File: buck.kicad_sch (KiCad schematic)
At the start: 32 parts, among them J6 Conn_01x02_Socket, Q1 RS1G120MNTB, Q2 RS1G120MNTB, U6 BQ24640

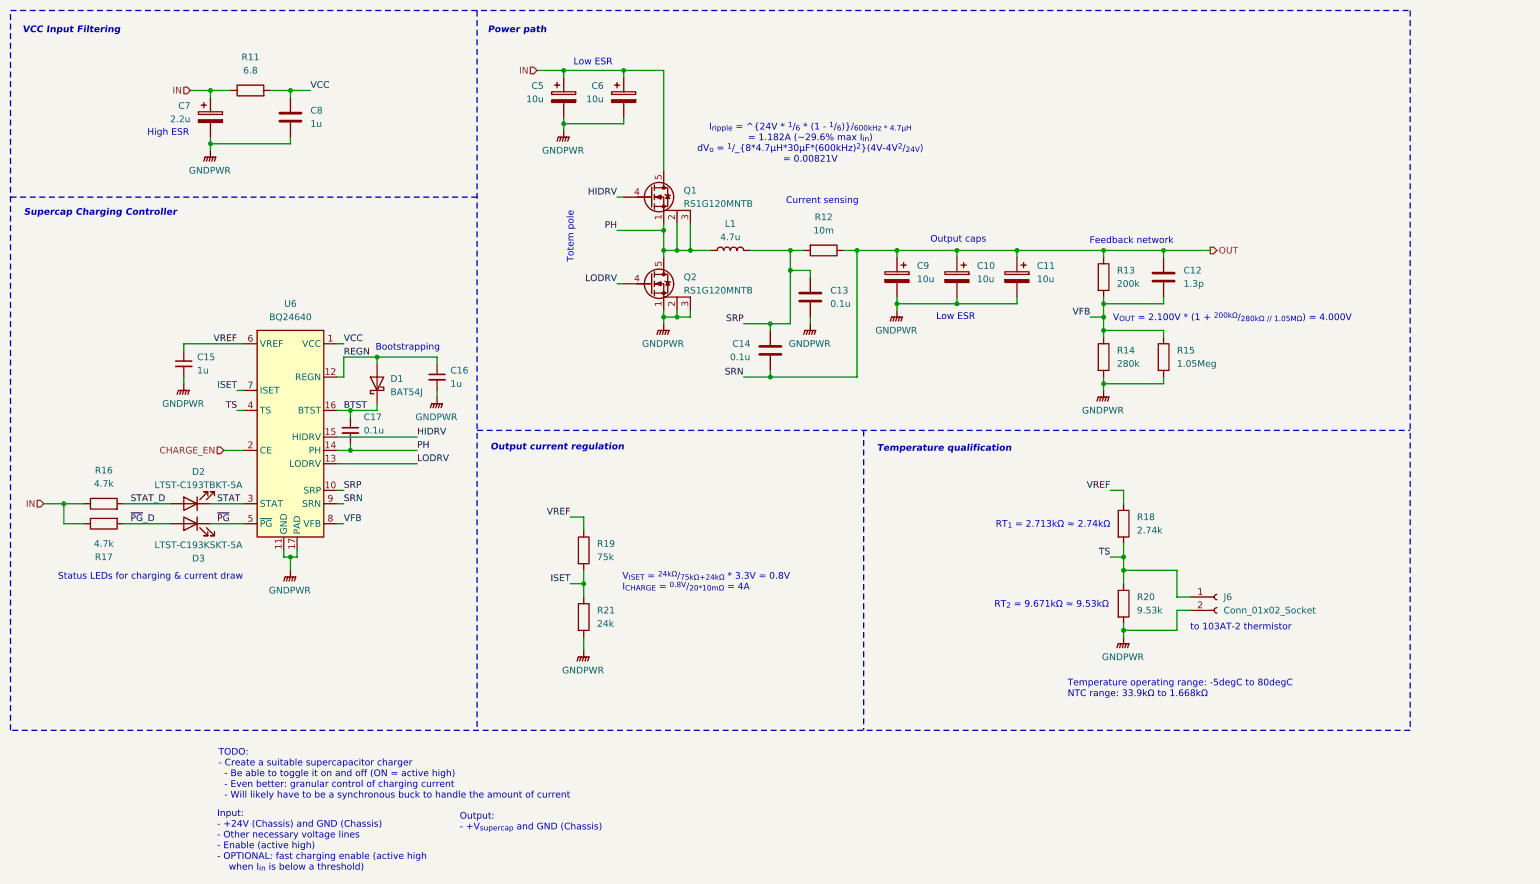
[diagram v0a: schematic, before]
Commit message: Tuned circuits & adjusted values
Changed footprints for some circuits to consolidate components
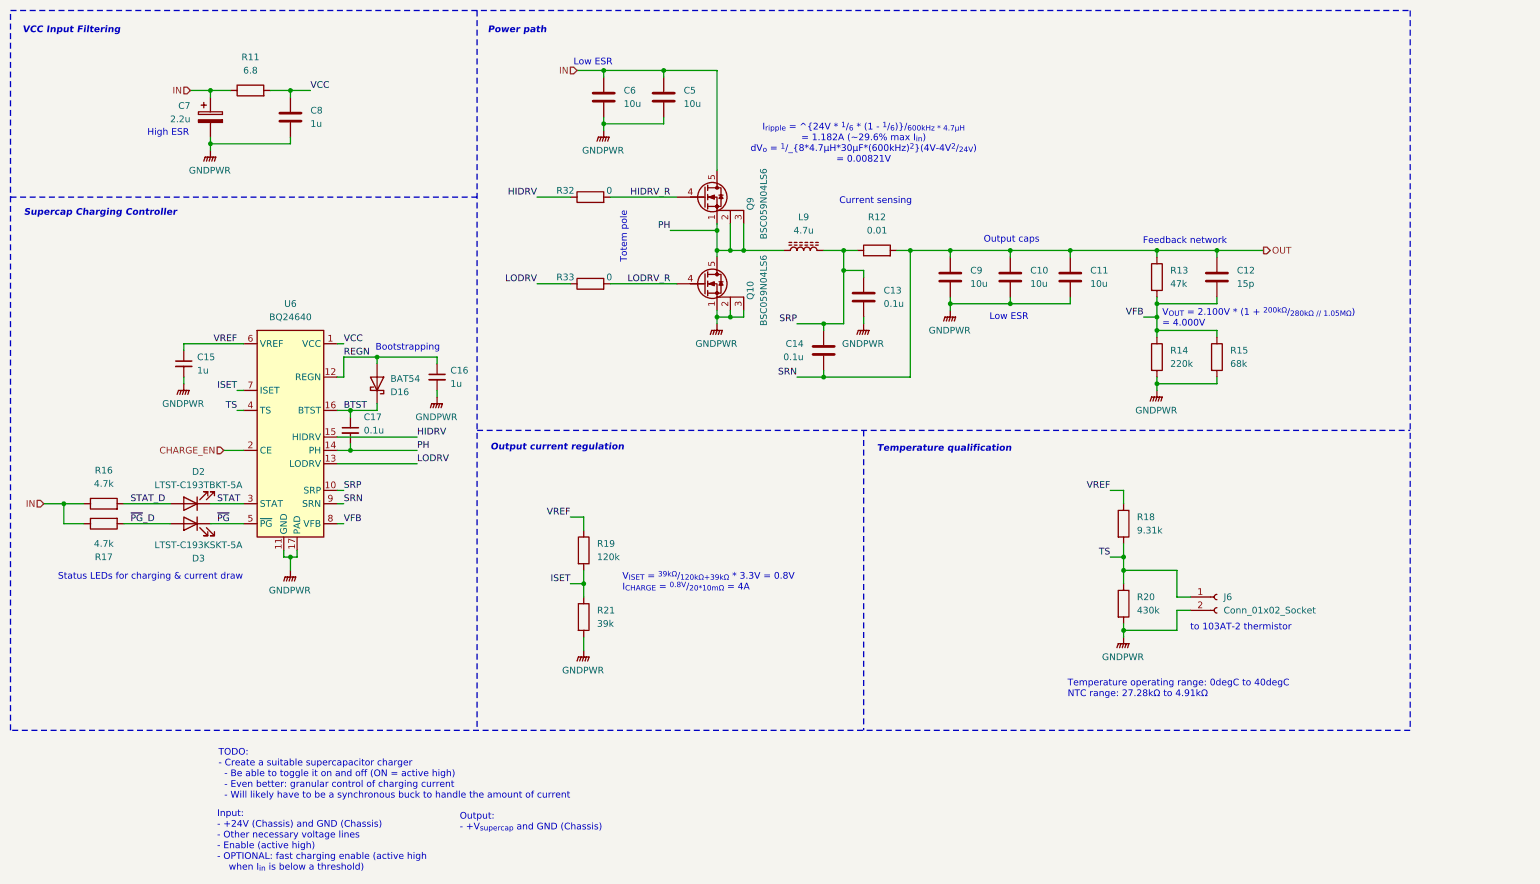
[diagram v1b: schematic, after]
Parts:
- removed C10, C11, C5, C6, C9: 10u, Capacitor_THT:CP_Radial_D5.0mm_P2.00mm, symbol Device:C_Polarized
- removed D1: BAT54J, Diode_SMD:D_SOD-323F, symbol Diode:BAT54J
- removed L1: 4.7u, Inductor_SMD:L_0603_1608Metric_Pad1.05x0.95mm_HandSolder, symbol Device:L
- removed Q1, Q2: RS1G120MNTB, Package_SO:PowerPAK_SO-8_Single, symbol Device:Q_NMOS_SGD
- added C10, C11, C5, C6, C9: 10u, Capacitor_SMD:C_0805_2012Metric_Pad1.18x1.45mm_HandSolder, symbol Device:C
- added D16: BAT54, Package_TO_SOT_SMD:SOT-23_Handsoldering, symbol Device:D_Schottky
- added L9: 4.7u, Inductor_SMD:L_Bourns_SRN8040TA, symbol Device:L_Ferrite
- added Q10, Q9: BSC059N04LS6, Package_SON:Infineon_PG-TDSON-8_6.15x5.15mm, symbol Transistor_FET:Q_NMOS_SGD
- added R32, R33: 0, Resistor_SMD:R_0603_1608Metric_Pad0.98x0.95mm_HandSolder, symbol Device:R
- C12: value 1.3p -> 15p
- C7: footprint Capacitor_SMD:C_0603_1608Metric_Pad1.08x0.95mm_HandSolder -> Capacitor_THT:C_Radial_D5.0mm_H11.0mm_P2.00mm; Mouser Part Number (none) -> 710-860010672006
- R12: value 10m -> 0.01; footprint Resistor_SMD:R_0603_1608Metric_Pad0.98x0.95mm_HandSolder -> Resistor_SMD:R_0612_1632Metric_Pad1.18x3.40mm_HandSolder; Mouser Part Number (none) -> 652-CFG0612FXR010ELF
- R13: value 200k -> 47k
- R14: value 280k -> 220k
- R15: value 1.05Meg -> 68k
- R18: value 2.74k -> 9.31k
- R19: value 75k -> 120k
- R20: value 9.53k -> 430k
- R21: value 24k -> 39k
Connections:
- net BTST: now also D16.3 (K)
- net GNDPWR: now also C10.2, C11.2, C5.2, C6.2, C9.2, Q10.1 (S), Q10.2 (S), Q10.3 (S)
- net HIDRV: now also R32.1
- net IN: now also C5.1, C6.1, Q9.5 (D)
- net LODRV: now also R33.1
- net OUT: now also R12.2, C10.1, C11.1, C9.1; no longer R12.1
- net PH: now also L9.1, Q10.5 (D), Q9.1 (S), Q9.2 (S), Q9.3 (S)
- net REGN: now also D16.1 (A)
- net SRP: now also R12.1, L9.2; no longer R12.2
- new net HIDRV_R: Q9.4 (G), R32.2
- new net LODRV_R: Q10.4 (G), R33.2
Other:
- note added: "Temperature operating range: 0degC to 40degC NTC range: 27.28kΩ to 4.91kΩ"
- note added: "V_{ISET} = ^{39kΩ}/_{120kΩ+39kΩ} * 3.3V = 0.8V I_{CHARGE} = ^{0.8V}/_{20*10mΩ} = 4A"
- note removed: "RT_{1} = 2.713kΩ ≈ 2.74kΩ"
- note removed: "RT_{2} = 9.671kΩ ≈ 9.53kΩ"
- note removed: "Temperature operating range: -5degC to 80degC NTC range: 33.9kΩ to 1.668kΩ"
- note removed: "V_{ISET} = ^{24kΩ}/_{75kΩ+24kΩ} * 3.3V = 0.8V I_{CHARGE} = ^{0.8V}/_{20*10mΩ} = 4A"
- moved on the sheet: C12, C13, C14, R13, R14, R15

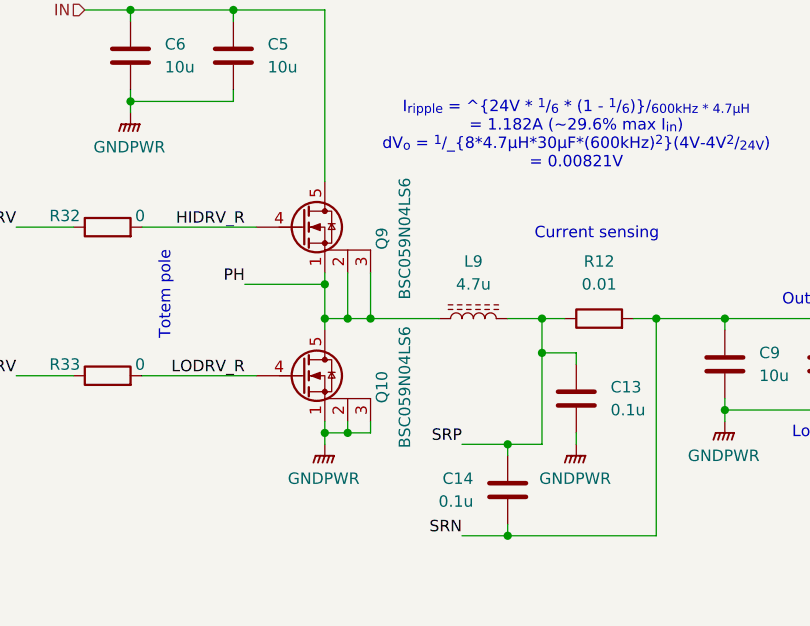
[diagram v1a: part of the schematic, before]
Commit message: Redesigning output boosts to be more efficient albeit with less current capacity
idk what I changed with the schematics lol
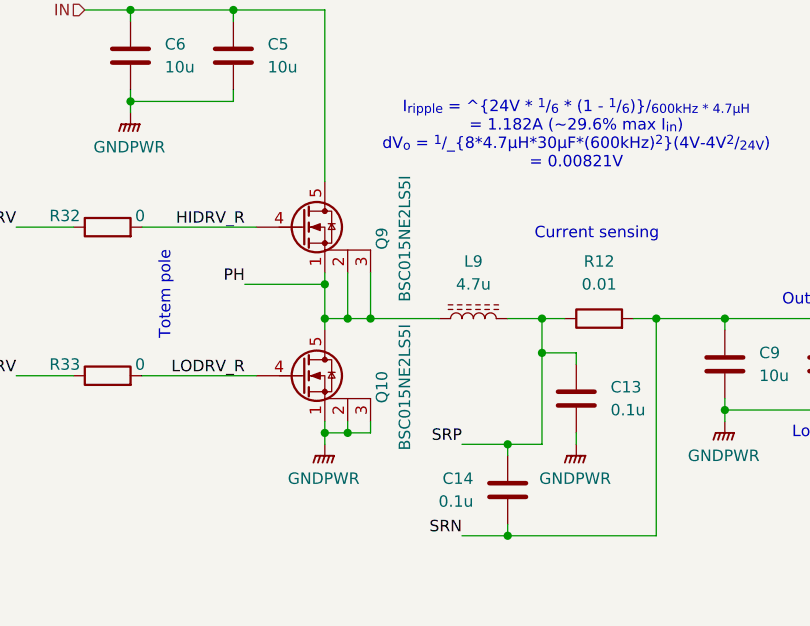
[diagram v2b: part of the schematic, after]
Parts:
- Q10, Q9: value BSC059N04LS6 -> BSC015NE2LS5I; Mouser Part Number 726-BSC059N04LS6ATMA -> 726-BSC015NE2LS5IATM
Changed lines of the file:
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@@
 			)
 		)
-		(property "Value" "BSC059N04LS6"
+		(property "Value" "BSC015NE2LS5I"
 			(at 157.48 60.96 90)
 			(effects
@@
 			)
 		)
-		(property "Datasheet" "https://www.mouser.com/datasheet/2/196/Infineon_BSC059N04LS6_DataSheet_v02_01_EN-3360636.pdf"
+		(property "Datasheet" "https://www.mouser.com/datasheet/2/196/Infineon_BSC015NE2LS5I_DataSheet_v02_01_EN-3360635.pdf"
 			(at 146.05 59.69 0)
 			(effects
@@
 			)
 		)
-		(property "Mouser Part Number" "726-BSC059N04LS6ATMA"
+		(property "Mouser Part Number" "726-BSC015NE2LS5IATM"
 			(at 146.05 59.69 0)
 			(effects
@@
 			)
 		)
-		(property "Value" "BSC059N04LS6"
+		(property "Value" "BSC015NE2LS5I"
 			(at 157.48 77.47 90)
 			(effects
@@
 			)
 		)
-		(property "Datasheet" "https://www.mouser.com/datasheet/2/196/Infineon_BSC059N04LS6_DataSheet_v02_01_EN-3360636.pdf"
+		(property "Datasheet" "https://www.mouser.com/datasheet/2/196/Infineon_BSC015NE2LS5I_DataSheet_v02_01_EN-3360635.pdf"
 			(at 146.05 76.2 0)
 			(effects
@@
 			)
 		)
-		(property "Mouser Part Number" "726-BSC059N04LS6ATMA"
+		(property "Mouser Part Number" "726-BSC015NE2LS5IATM"
 			(at 146.05 76.2 0)
 			(effects

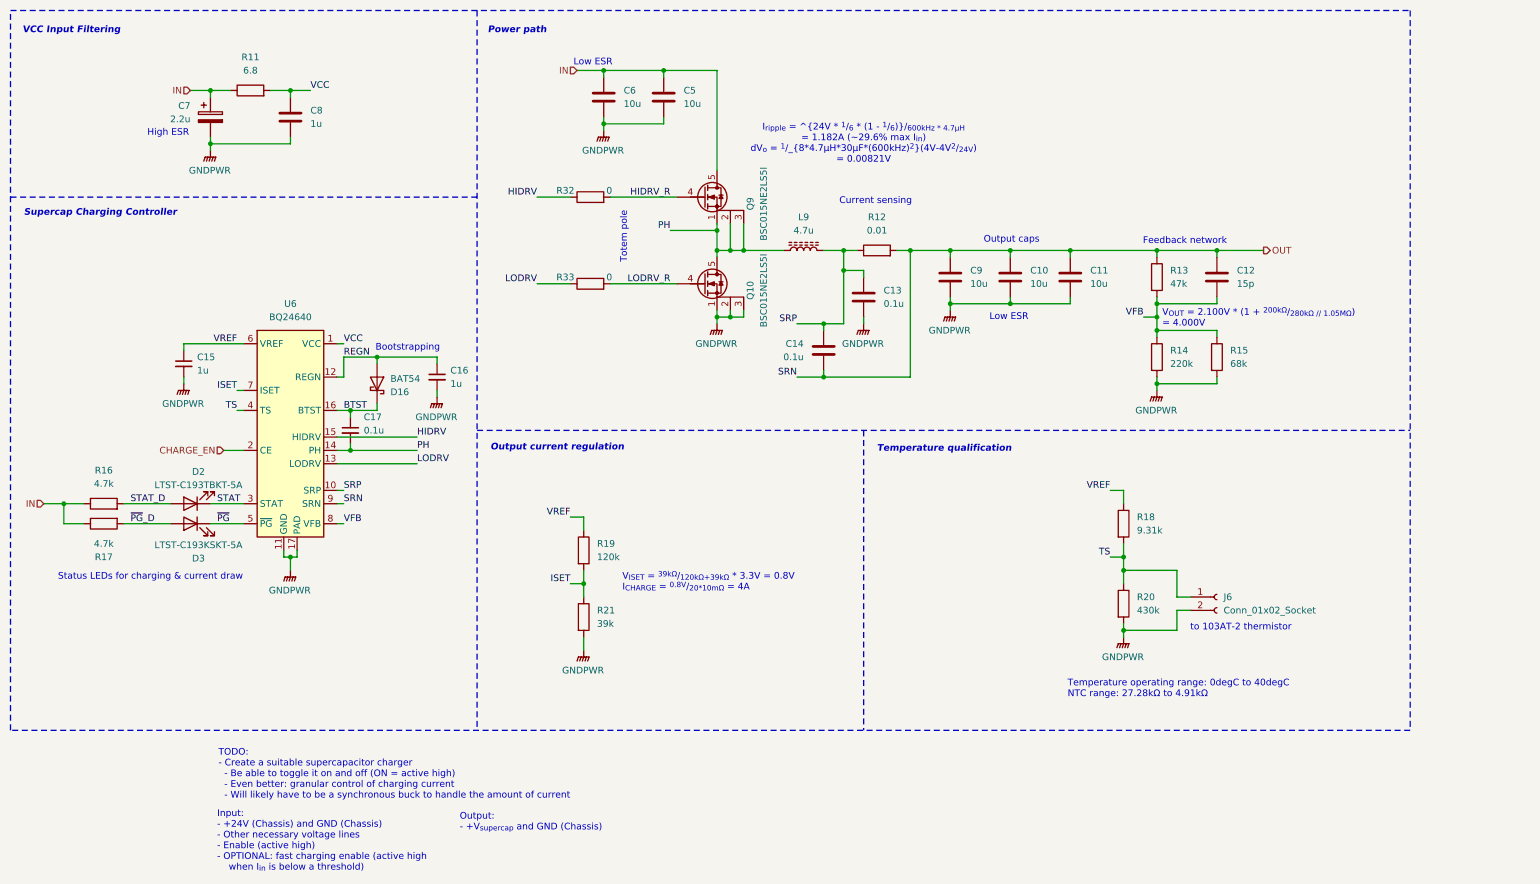
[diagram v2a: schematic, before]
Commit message: Up charging current to 6A
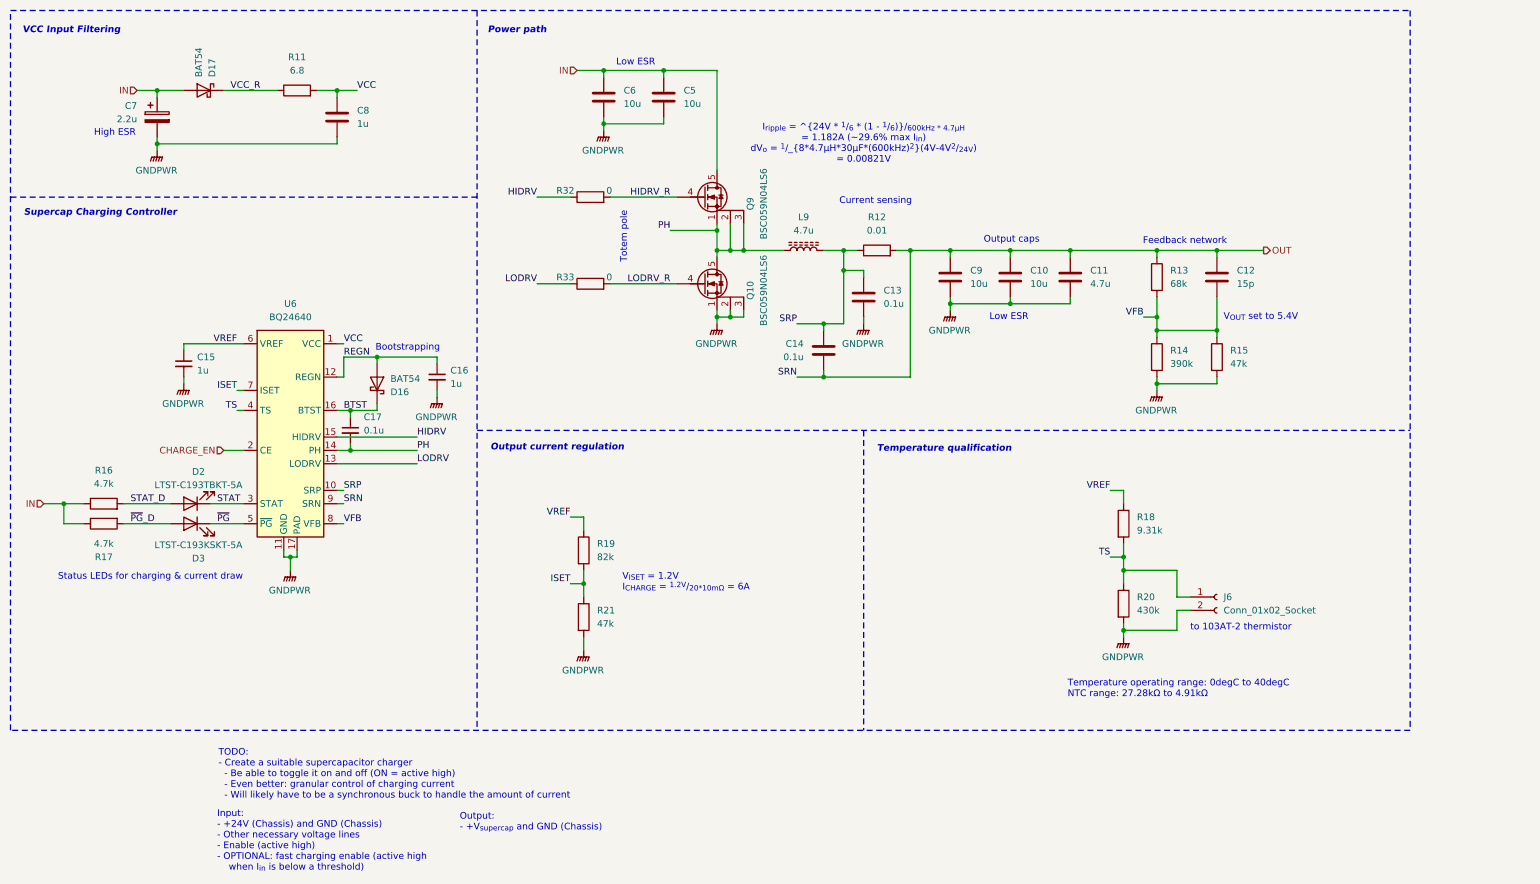
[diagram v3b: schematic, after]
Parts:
- added D17: BAT54, Package_TO_SOT_SMD:SOT-23_Handsoldering, symbol Device:D_Schottky
- C11: value 10u -> 4.7u
- Q10, Q9: value BSC015NE2LS5I -> BSC059N04LS6; Mouser Part Number 726-BSC015NE2LS5IATM -> 726-BSC059N04LS6ATMA
- R13: value 47k -> 68k
- R14: value 220k -> 390k
- R15: value 68k -> 47k
- R19: value 120k -> 82k
- R21: value 39k -> 47k
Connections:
- net IN: now also D17.1 (A); no longer R11.1
- new net VCC_R: D17.3 (K), R11.1
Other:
- note added: "V_{ISET} = 1.2V I_{CHARGE} = ^{1.2V}/_{20*10mΩ} = 6A"
- note added: "V_{OUT} set to 5.4V"
- note removed: "V_{ISET} = ^{39kΩ}/_{120kΩ+39kΩ} * 3.3V = 0.8V I_{CHARGE} = ^{0.8V}/_{20*10mΩ} = 4A"
- note removed: "V_{OUT} = 2.100V * (1 + ^{200kΩ}/_{280kΩ // 1.05MΩ}) = 4.000V"
- moved on the sheet: C7, C8, R11

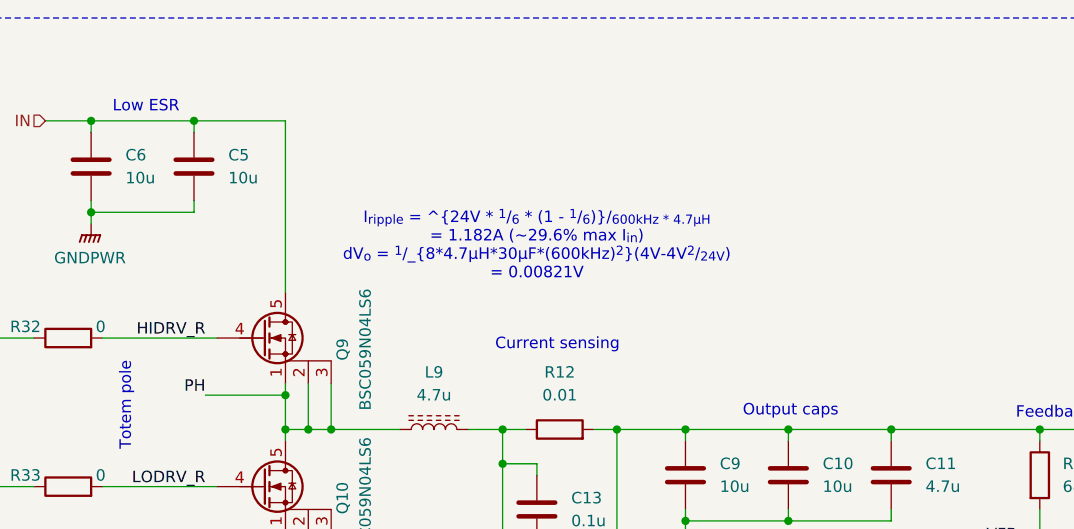
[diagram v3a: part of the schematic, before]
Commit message: Add supercaps subsheets
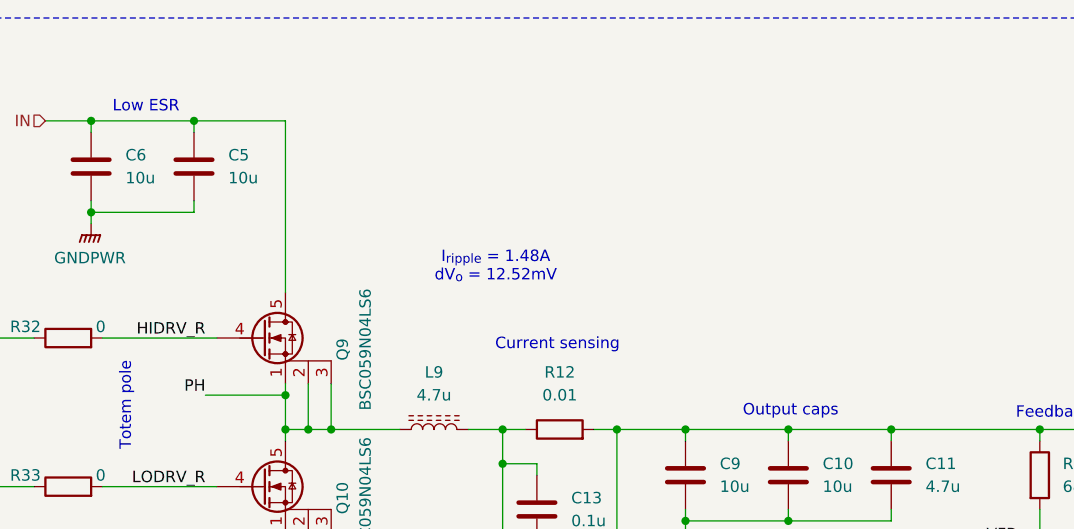
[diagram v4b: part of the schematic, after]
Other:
- note added: "I_{ripple} = 1.48A dV_{o} = 12.52mV"
- note removed: "I_{ripple} = ^{24V * ^{1}/_{6} * (1 - ^{1}/_{6})}/_{600kHz * 4.7µH} = 1.182A (~29.6% max I_{in}) dV_{o} = ^{1}/_{8*4.7µH*30µF*(600kHz)^{2}}(4V-4V^{2}/_{24V}) = 0.00821V"
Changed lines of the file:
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@@
 		)
 	)
-	(text "I_{ripple} = ^{24V * ^{1}/_{6} * (1 - ^{1}/_{6})}/_{600kHz * 4.7µH}\n= 1.182A (~29.6% max I_{in})\ndV_{o} = ^{1}/_{8*4.7µH*30µF*(600kHz)^{2}}(4V-4V^{2}/_{24V})\n= 0.00821V"
+	(text "I_{ripple} = 1.48A\ndV_{o} = 12.52mV"
 		(exclude_from_sim no)
-		(at 176.53 49.53 0)
+		(at 171.958 51.816 0)
 		(effects
 			(font
